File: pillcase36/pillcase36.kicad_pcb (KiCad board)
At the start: 2 copper layers, 114 x 140.5 mm, 125 parts, among them J1 AudioJack4_Ground, SW1 SW_Push, SW10 SW_Push, SW11 SW_Push, SW12 SW_Push, SW13 SW_Push, SW14 SW_Push, SW15 SW_Push, SW16 SW_Push, SW17 SW_Push, SW18 SW_Push, SW19 SW_Push, SW2 SW_Push, SW20 SW_Push, SW21 SW_Push, SW22 SW_Push, SW23 SW_Push, SW24 SW_Push, SW25 SW_Push, SW26 SW_Push, SW27 SW_Push, SW28 SW_Push, SW29 SW_Push, SW3 SW_Push, SW30 SW_Push, SW31 SW_Push, SW32 SW_Push, SW33 SW_Push, SW34 SW_Push, SW35 SW_Push, SW36 SW_Push, SW37 SW_Push, SW4 SW_Push, SW5 SW_Push, SW6 SW_Push, SW7 SW_Push, SW8 SW_Push, SW9 SW_Push, U1 BlackPill, U2 24LC00

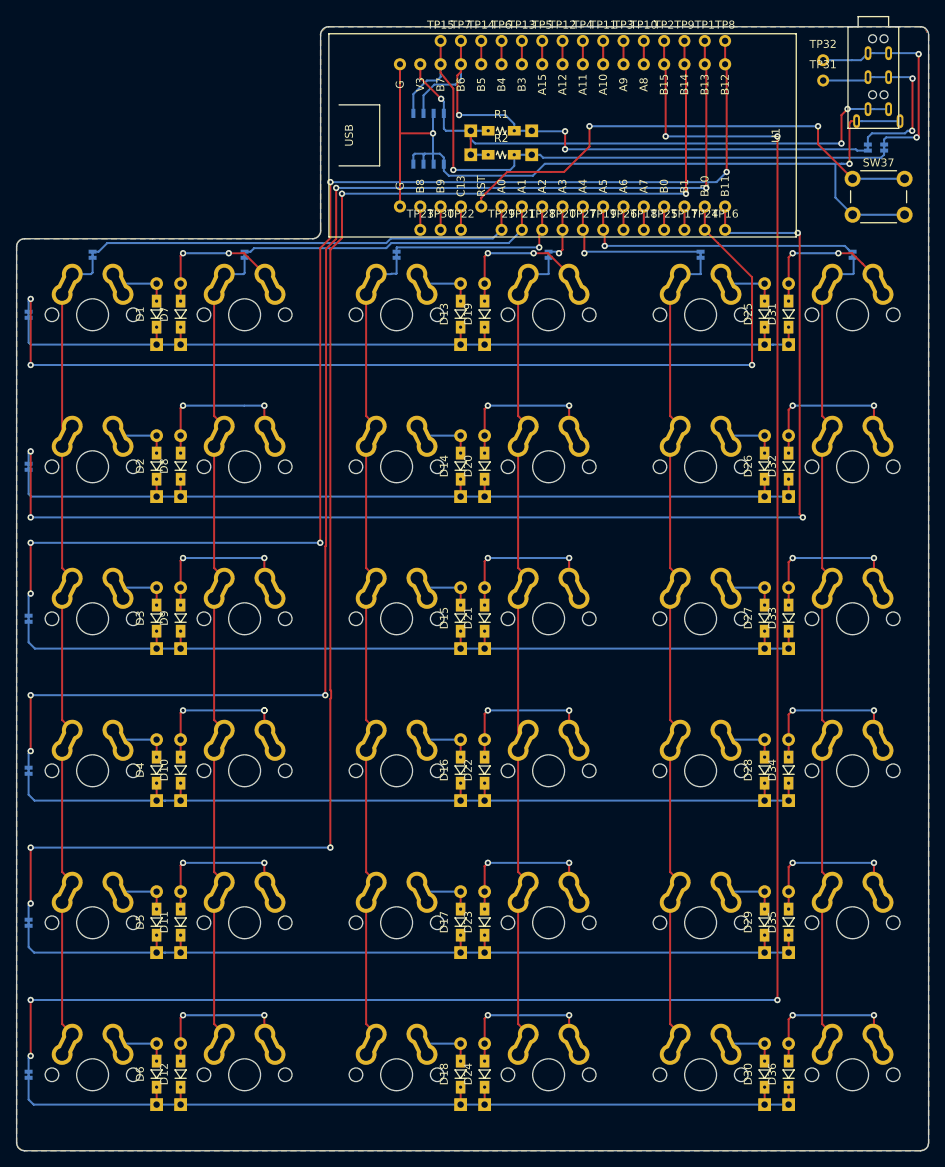
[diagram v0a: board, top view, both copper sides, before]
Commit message: Quick trace cleanup
- Aesthetic changes
- Via reduction
- Reduction of right angle traces
- Move traces away from edge
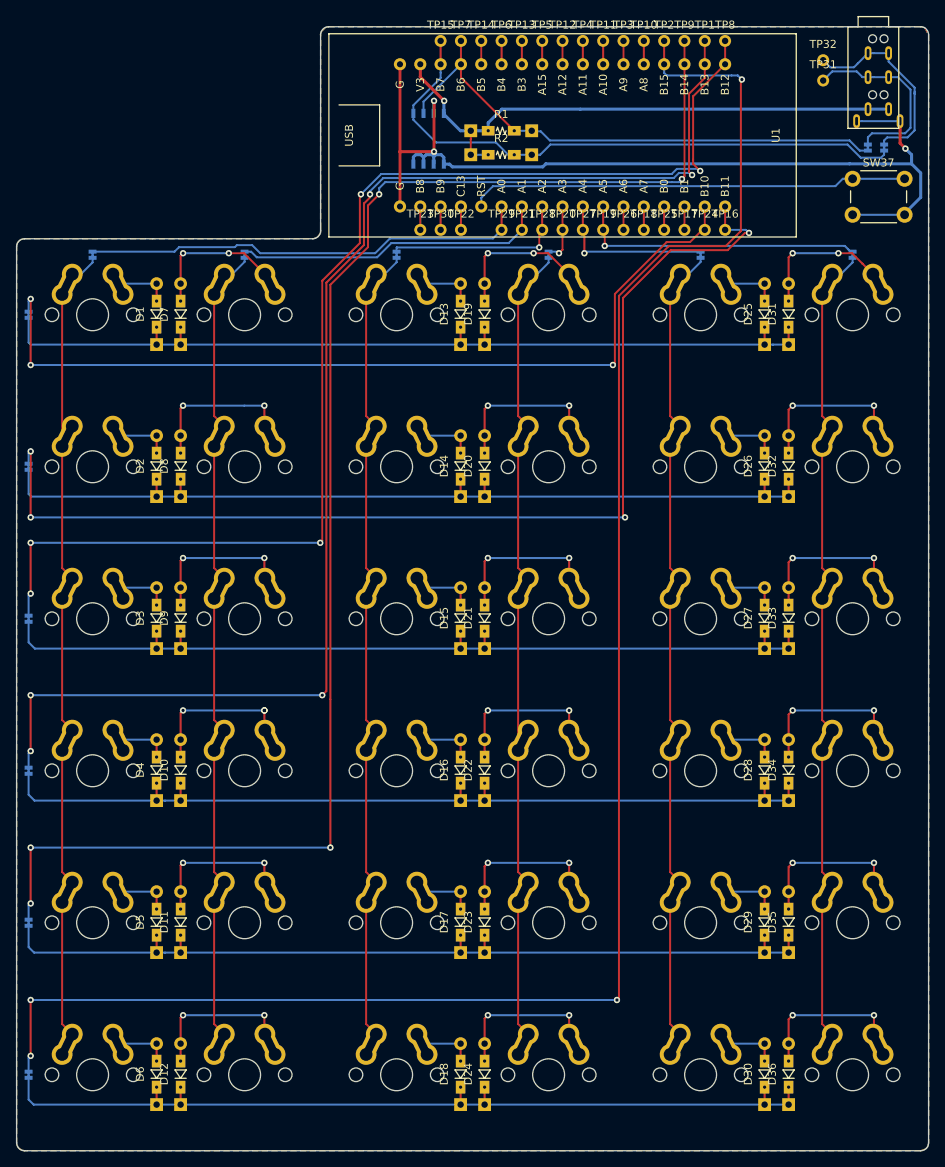
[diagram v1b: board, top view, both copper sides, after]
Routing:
- net ROW1: track 154.6 -> 137.1 mm
- net ROW5: track 236.5 -> 222.3 mm, vias 5 -> 4
- net ROW0: track 122.6 -> 109.4 mm
- net GND: track 113.7 -> 123.0 mm, vias 2 -> 3
- net RESET: track 63.2 -> 55.0 mm, vias 2 -> 0
- net SDA1: track 81.4 -> 74.0 mm, vias 1 -> 0
- net VCC: track 77.5 -> 70.8 mm, vias 3 -> 1
- net SCL1: track 74.1 -> 67.5 mm, vias 3 -> 0
- net ROW3: track 174.9 -> 170.3 mm
- net ROW2: track 157.7 -> 153.4 mm
- net ROW4: track 191.4 -> 187.7 mm
- net Net-(J1-PadR2): track 27.5 -> 25.2 mm, vias 2 -> 0
- net Net-(J1-PadR1): track 24.6 -> 23.6 mm, vias 2 -> 0
- net COL0: track 55.4 -> 56.2 mm
- net Net-(JP9-Pad2): track 89.3 -> 88.6 mm
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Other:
- net class Default: clearance 0.2 -> 0.2032
- net class Power added: clearance 0.2032, trace_width 0.381, via_dia 0.8, via_drill 0.4
- rule trace_clearance: 0.2 -> 0.2032

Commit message: Reroute row/col breakout
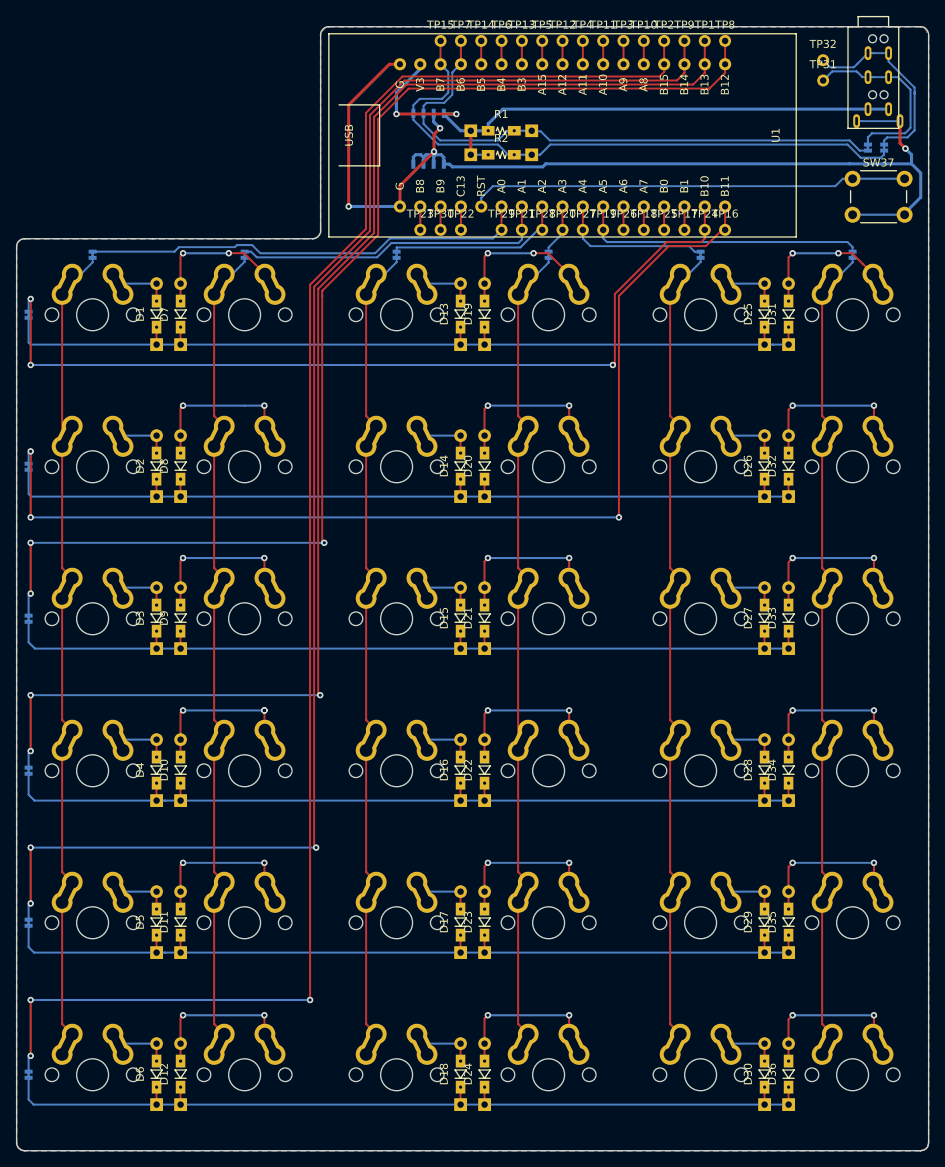
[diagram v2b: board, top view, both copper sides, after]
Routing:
- net ROW5: track 222.3 -> 202.2 mm, vias 4 -> 3
- net GND: track 123.0 -> 134.7 mm, vias 3 -> 4
- net VCC: track 70.8 -> 80.0 mm, vias 1 -> 2
- net ROW1: track 137.1 -> 130.9 mm, vias 4 -> 3
- net SCL1: track 67.5 -> 71.8 mm
- net SDA1: track 74.0 -> 76.4 mm
- net ROW4: track 187.7 -> 185.3 mm, vias 5 -> 3
- net ROW3: track 170.3 -> 168.4 mm, vias 5 -> 3
- net ROW2: track 153.4 -> 151.8 mm, vias 5 -> 3
- net COL4: track 20.7 -> 19.6 mm, vias 1 -> 0
- net COL2: track 23.8 -> 22.7 mm, vias 1 -> 0
- net COL3: track 7.59 -> 6.56 mm, vias 1 -> 0
- net COL1: track 39.5 -> 40.2 mm
- net ROW0: track 109.4 -> 110.0 mm
- net COL5: track 36.5 -> 36.4 mm, vias 1 -> 0
